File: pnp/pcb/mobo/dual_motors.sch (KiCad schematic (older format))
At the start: 9 parts, among them M5 MOTOR1, M6 MOTOR2

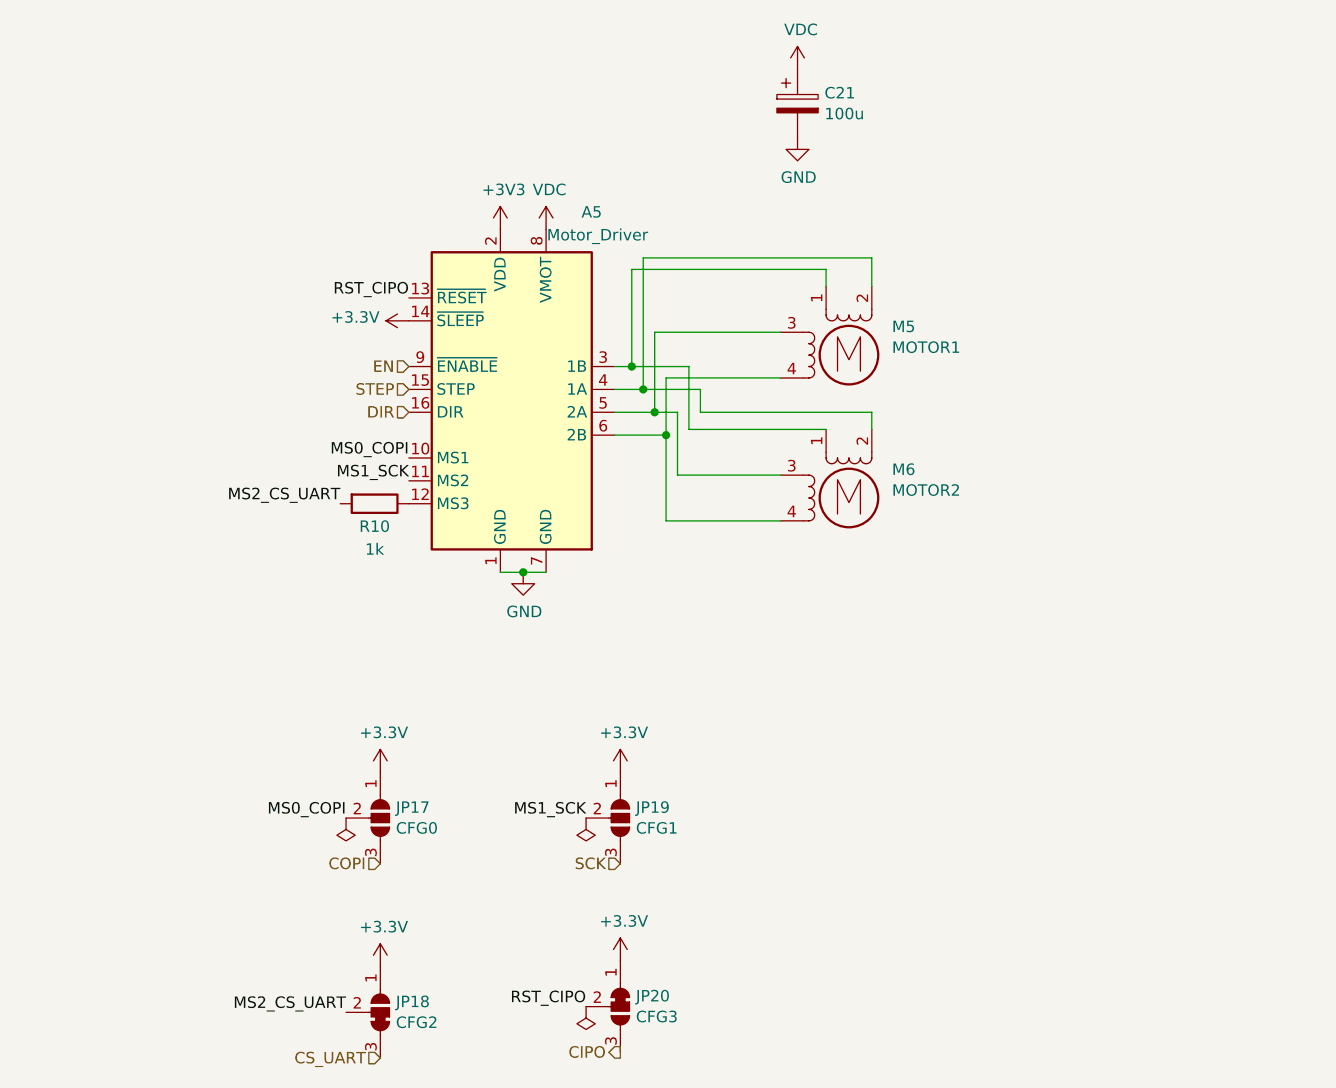
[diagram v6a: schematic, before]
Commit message: Schematic improvement proposal
Discord
@jessevdz

Fixes:
-Proper hierarchical structure
Label inside the sheets with their local name
Then connect them together at sheet-level.
- Split into functional blocks
Just like with software its good to have one function per group of components.
For example: the power input, reverse polarity protection, buckconverter, multiplexer and LDO
were connected as one block. Now they are split into their functional blocks.
- Used smaller symbols
Some symbols used their large variant, which looks a bit funny in normal schematics
For example some R's have been changed to R_Small's.
- Align symbols to grid
A lot of the symbols were off the default 50mil grid.

And a lot of other general fixes in readability and structure.
Electrically the schematic should be the same.
Improvements that would require a schematic change can possibly
be done later in a seperate commit.
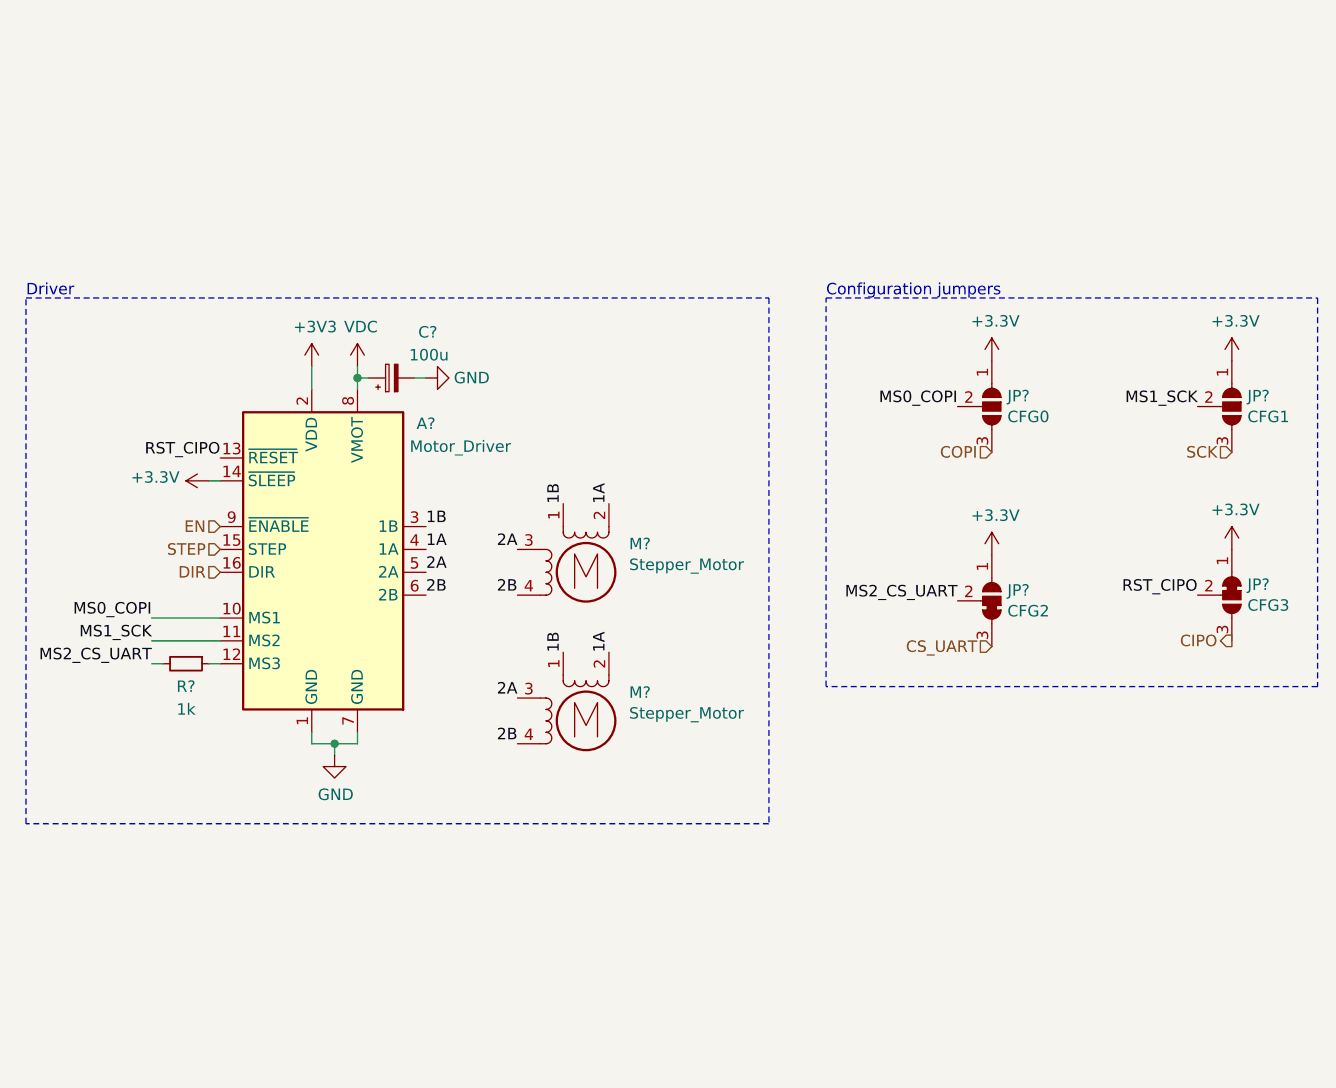
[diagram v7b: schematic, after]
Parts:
- removed A5: Motor_Driver, Module:Pololu_Breakout-16_15.2x20.3mm, symbol Driver_Motor:Pololu_Breakout_A4988
- removed C21: 100u, Capacitor_SMD:CP_Elec_6.3x7.7, symbol Device:CP
- removed JP17: CFG0, Jumper:SolderJumper-3_P1.3mm_Open_RoundedPad1.0x1.5mm, symbol Jumper:SolderJumper_3_Open
- removed JP19: CFG1, Jumper:SolderJumper-3_P1.3mm_Open_RoundedPad1.0x1.5mm, symbol Jumper:SolderJumper_3_Open
- removed JP20: CFG3, Jumper:SolderJumper-3_P1.3mm_Bridged12_RoundedPad1.0x1.5mm, symbol Jumper:SolderJumper_3_Bridged12
- removed JP22: CFG2, index:SolderJumper-3_P1.3mm_Bridged23_RoundedPad1.0x1.5mm, symbol index:SolderJumper_3_Bridged23
- removed M5: MOTOR1, Connector_JST:JST_XH_B4B-XH-A_1x04_P2.50mm_Vertical, symbol Motor:Stepper_Motor_bipolar
- removed M6: MOTOR2, Connector_JST:JST_XH_B4B-XH-A_1x04_P2.50mm_Vertical, symbol Motor:Stepper_Motor_bipolar
- removed R10: 1k, Resistor_SMD:R_0805_2012Metric, symbol Device:R
- added A?: Motor_Driver, Module:Pololu_Breakout-16_15.2x20.3mm, symbol Driver_Motor:Pololu_Breakout_A4988
- added C?: 100u, Capacitor_SMD:CP_Elec_6.3x7.7, symbol Device:CP_Small
- added JP?: CFG3, Jumper:SolderJumper-3_P1.3mm_Bridged12_RoundedPad1.0x1.5mm, symbol Jumper:SolderJumper_3_Bridged12
- added JP?: CFG1, Jumper:SolderJumper-3_P1.3mm_Open_RoundedPad1.0x1.5mm, symbol Jumper:SolderJumper_3_Open
- added JP?: CFG0, Jumper:SolderJumper-3_P1.3mm_Open_RoundedPad1.0x1.5mm, symbol Jumper:SolderJumper_3_Open
- added JP?: CFG2, index:SolderJumper-3_P1.3mm_Bridged23_RoundedPad1.0x1.5mm, symbol mobo-rescue:SolderJumper_3_Bridged23-index
- added M? (x2): Stepper_Motor, Connector_JST:JST_XH_B4B-XH-A_1x04_P2.50mm_Vertical, symbol Motor:Stepper_Motor_bipolar
- added R?: 1k, Resistor_SMD:R_0805_2012Metric, symbol Device:R_Small
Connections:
- net +3V3: now also A?.14 (~SLEEP), A?.2 (VDD), JP?.1 (A), JP?.1 (A), JP?.1 (A), JP?.1 (B)
- net CIPO: now also JP?.3 (B)
- net COPI: now also JP?.3 (B)
- net CS_UART: now also JP?.3 (A)
- net DIR: now also A?.16 (DIR)
- net EN: now also A?.9 (~ENABLE)
- net GND: now also A?.1 (GND), A?.7 (GND), C?.2
- net MS0_COPI: now also A?.10 (MS1), JP?.2 (C)
- net MS1_SCK: now also A?.11 (MS2), JP?.2 (C)
- net MS2_CS_UART: now also JP?.2 (C), R?.2
- net RST_CIPO: now also A?.13 (~RESET), JP?.2 (C)
- net SCK: now also JP?.3 (B)
- net STEP: now also A?.15 (STEP)
- net VDC: now also A?.8 (VMOT), C?.1
- new net: A?.12 (MS3), R?.1
- new net 1A: A?.4 (1A), M?.2 (-), M?.2 (-)
- new net 1B: A?.3 (1B), M?.1, M?.1
- new net 2A: A?.5 (2A), M?.3, M?.3
- new net 2B: A?.6 (2B), M?.4, M?.4
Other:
- note added: "Configuration jumpers"
- note added: "Driver"
